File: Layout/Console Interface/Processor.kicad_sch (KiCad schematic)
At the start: 26 parts, among them J1 USB_C_Receptacle_USB2.0, SW1 SW_BOOT, U1 W25Q32JVSS, U2 RP2040, Y1 Crystal_GND24

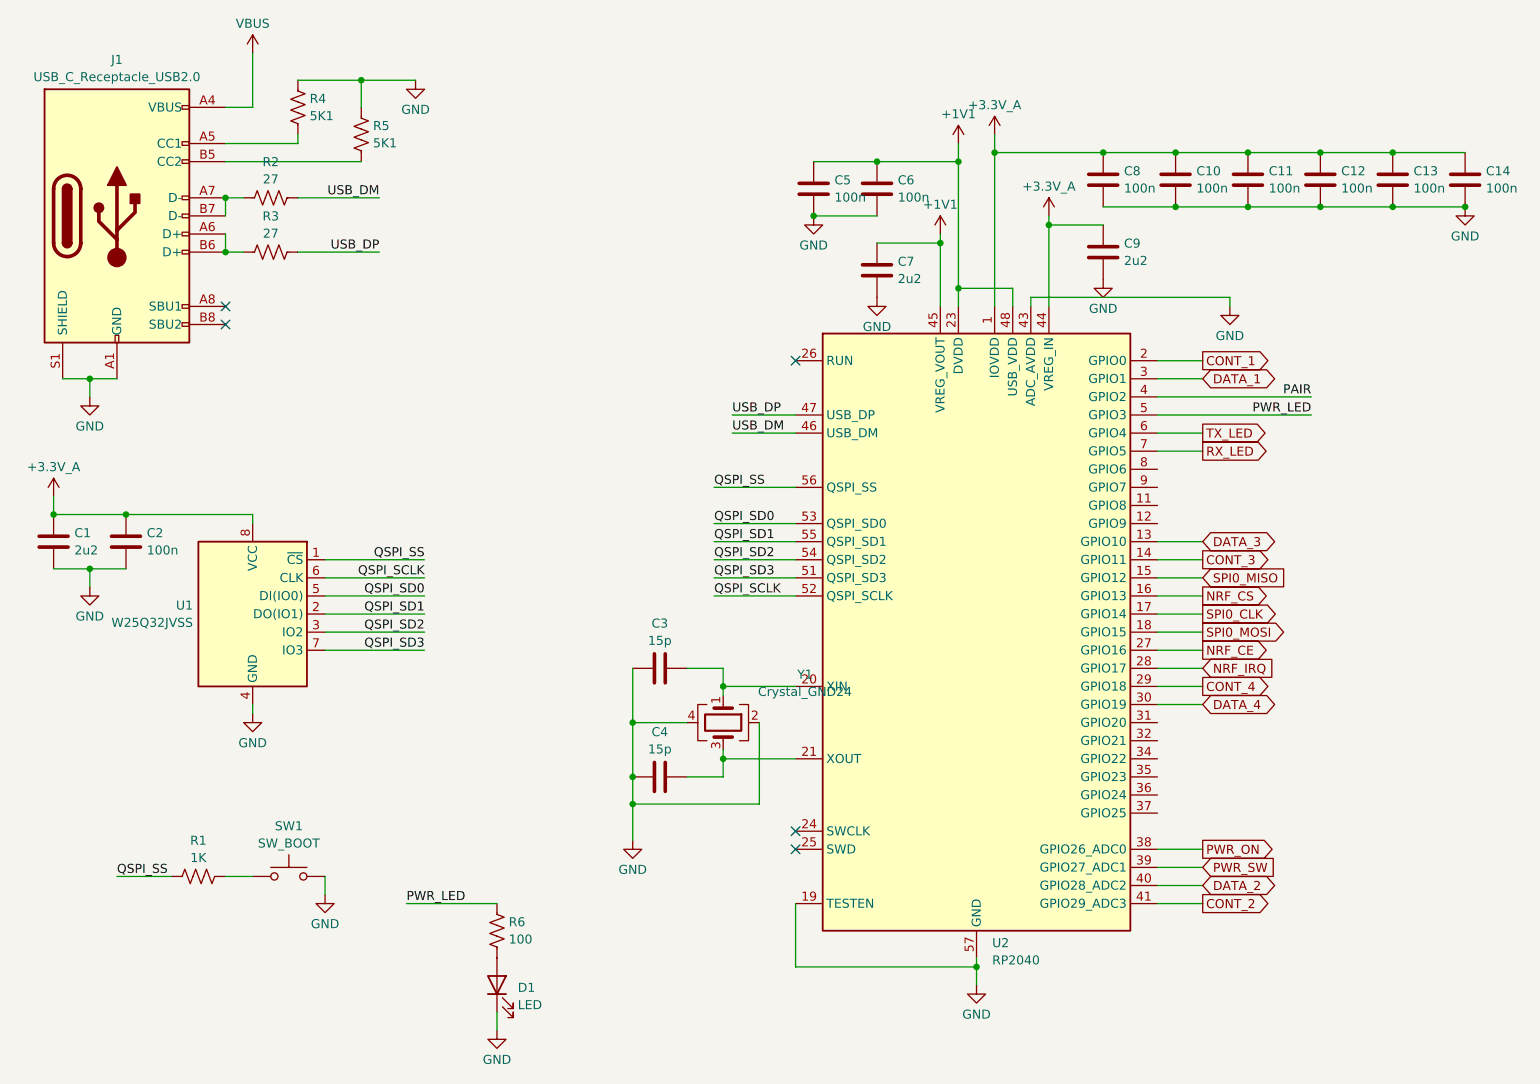
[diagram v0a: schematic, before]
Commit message: Add console interface schematic
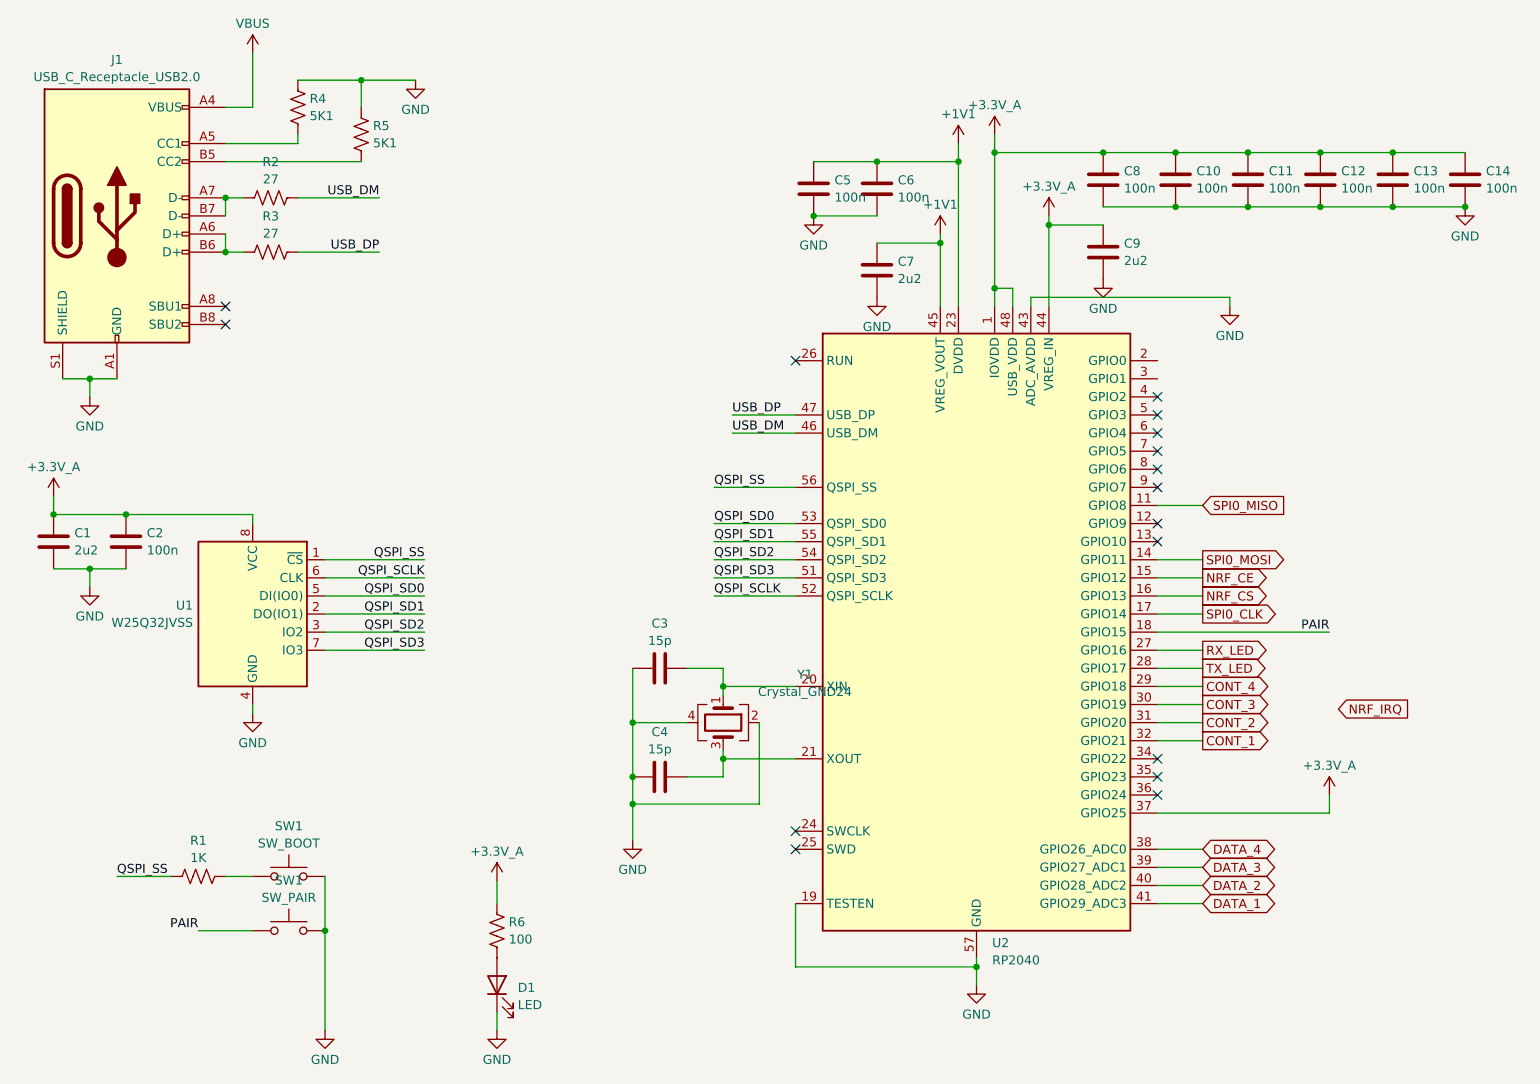
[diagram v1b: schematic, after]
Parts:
- added SW1: SW_PAIR, Button_Switch_SMD:SW_SPST_B3U-3000P, symbol Switch:SW_Push
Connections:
- net PWR_ON is gone; now on net DATA_4: U2.38 (GPIO26_ADC0)
- net PWR_SW is gone; now on net DATA_3: U2.39 (GPIO27_ADC1)
- net +1V1: no longer U2.48 (USB_VDD)
- net +3.3V_A: now also R6.1, U2.37 (GPIO25), U2.48 (USB_VDD)
- net CONT_1: now also U2.32 (GPIO21); no longer U2.2 (GPIO0)
- net CONT_2: now also U2.31 (GPIO20); no longer U2.41 (GPIO29_ADC3)
- net CONT_3: now also U2.30 (GPIO19); no longer U2.14 (GPIO11)
- net DATA_1: now also U2.41 (GPIO29_ADC3); no longer U2.3 (GPIO1)
- net DATA_3: no longer U2.13 (GPIO10)
- net DATA_4: no longer U2.30 (GPIO19)
- net GND: now also SW1.2
- net NRF_CE: now also U2.15 (GPIO12); no longer U2.27 (GPIO16)
- net NRF_IRQ: no longer U2.28 (GPIO17)
- net PAIR: now also U2.18 (GPIO15), SW1.1; no longer U2.4 (GPIO2)
- net RX_LED: now also U2.27 (GPIO16); no longer U2.7 (GPIO5)
- net SPI0_MISO: now also U2.11 (GPIO8); no longer U2.15 (GPIO12)
- net SPI0_MOSI: now also U2.14 (GPIO11); no longer U2.18 (GPIO15)
- net TX_LED: now also U2.28 (GPIO17); no longer U2.6 (GPIO4)
- net PWR_LED: no longer names the net of U2.5 (GPIO3)
- net PWR_LED: no longer R6.1
- no-connect marks 5 -> 16

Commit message: Use separate board for lights
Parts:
- D1: footprint LED_SMD:LED_0805_2012Metric -> LED_SMD:LED_0603_1608Metric
- R6: footprint Resistor_SMD:R_0805_2012Metric -> Resistor_SMD:R_0603_1608Metric
- SW1: footprint Button_Switch_SMD:SW_SPST_B3U-3000P -> Button_Switch_SMD:Panasonic_EVQPUK_EVQPUB
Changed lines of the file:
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@@
       (effects (font (size 1.27 1.27)))
     )
-    (property "Footprint" "Button_Switch_SMD:SW_SPST_B3U-3000P" (at 81.28 140.97 0)
+    (property "Footprint" "Button_Switch_SMD:Panasonic_EVQPUK_EVQPUB" (at 81.28 140.97 0)
       (effects (font (size 1.27 1.27)) hide)
     )
@@
       (effects (font (size 1.27 1.27)) (justify right))
     )
-    (property "Footprint" "LED_SMD:LED_0805_2012Metric" (at 110.49 153.67 0)
+    (property "Footprint" "LED_SMD:LED_0603_1608Metric" (at 110.49 153.67 0)
       (effects (font (size 1.27 1.27)) hide)
     )
@@
       (effects (font (size 1.27 1.27)) (justify left))
     )
-    (property "Footprint" "Resistor_SMD:R_0805_2012Metric" (at 111.506 146.304 90)
-      (effects (font (size 1.27 1.27)) hide)
-    )
+    (property "Footprint" "Resistor_SMD:R_0603_1608Metric" (at 111.506 146.304 90)
+      (effects (font (size 1.27 1.27)) hide)
+    )
